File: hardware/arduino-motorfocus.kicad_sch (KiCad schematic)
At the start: 23 parts, among them J1 Motor, J2 PWR_MOTOR, J3 Debug, J4 I2C, J5 STEPS, J6 ULN2003A, J7 PWR_MOTOR, SW1 IN, SW2 OUT, SW3 WIN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

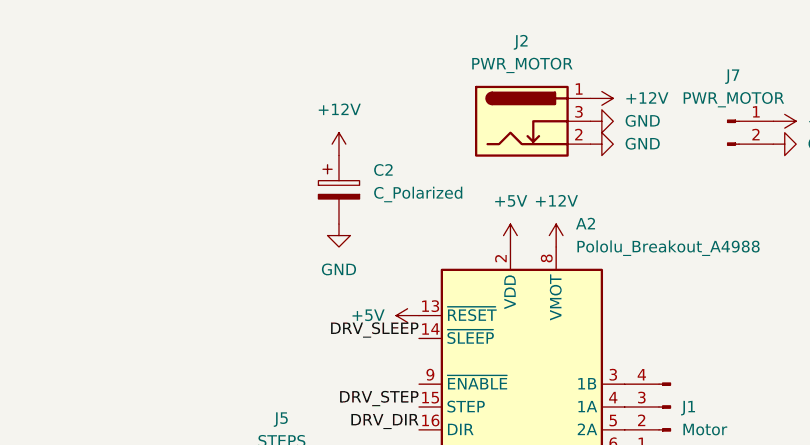
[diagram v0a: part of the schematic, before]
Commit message: Added simple PCB project and doc
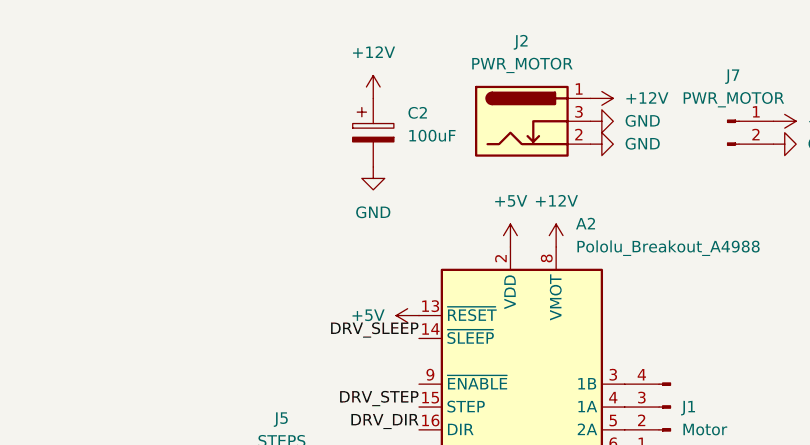
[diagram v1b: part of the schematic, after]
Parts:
- C2: value C_Polarized -> 100uF
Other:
- moved on the sheet: C2
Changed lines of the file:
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@@
     )
   )
-  (symbol (lib_id "Device:C_Polarized") (at 199.39 39.37 0) (unit 1)
-    (in_bom yes) (on_board yes) (dnp no) (fields_autoplaced)
-    (property "Reference" "C2" (at 203.2 37.211 0)
-      (effects (font (size 1.27 1.27)) (justify left))
-    )
-    (property "Value" "C_Polarized" (at 203.2 39.751 0)
-      (effects (font (size 1.27 1.27)) (justify left))
-    )
-    (property "Footprint" "Capacitor_SMD:CP_Elec_6.3x5.9" (at 200.3552 43.18 0)
-      (effects (font (size 1.27 1.27)) hide)
-    )
-    (property "Datasheet" "~" (at 199.39 39.37 0)
+  (symbol (lib_id "Device:C_Polarized") (at 203.2 33.02 0) (unit 1)
+    (in_bom yes) (on_board yes) (dnp no) (fields_autoplaced)
+    (property "Reference" "C2" (at 207.01 30.861 0)
+      (effects (font (size 1.27 1.27)) (justify left))
+    )
+    (property "Value" "100uF" (at 207.01 33.401 0)
+      (effects (font (size 1.27 1.27)) (justify left))
+    )
+    (property "Footprint" "Capacitor_SMD:CP_Elec_6.3x5.9" (at 204.1652 36.83 0)
+      (effects (font (size 1.27 1.27)) hide)
+    )
+    (property "Datasheet" "~" (at 203.2 33.02 0)
       (effects (font (size 1.27 1.27)) hide)
     )
@@
     )
   )
-  (symbol (lib_id "power:GND") (at 199.39 43.18 0) (unit 1)
-    (in_bom yes) (on_board yes) (dnp no) (fields_autoplaced)
-    (property "Reference" "#PWR019" (at 199.39 49.53 0)
-      (effects (font (size 1.27 1.27)) hide)
-    )
-    (property "Value" "GND" (at 199.39 48.26 0)
-      (effects (font (size 1.27 1.27)))
-    )
-    (property "Footprint" "" (at 199.39 43.18 0)
-      (effects (font (size 1.27 1.27)) hide)
-    )
-    (property "Datasheet" "" (at 199.39 43.18 0)
+  (symbol (lib_id "power:GND") (at 203.2 36.83 0) (unit 1)
+    (in_bom yes) (on_board yes) (dnp no) (fields_autoplaced)
+    (property "Reference" "#PWR019" (at 203.2 43.18 0)
+      (effects (font (size 1.27 1.27)) hide)
+    )
+    (property "Value" "GND" (at 203.2 41.91 0)
+      (effects (font (size 1.27 1.27)))
+    )
+    (property "Footprint" "" (at 203.2 36.83 0)
+      (effects (font (size 1.27 1.27)) hide)
+    )
+    (property "Datasheet" "" (at 203.2 36.83 0)
       (effects (font (size 1.27 1.27)) hide)
     )
@@
       (effects (font (size 1.27 1.27)) hide)
     )
-    (property "Datasheet" "~" (at 220.98 32.766 0)
+    (property "Datasheet" "https://de.aliexpress.com/item/1005002561919358.html" (at 220.98 32.766 0)
       (effects (font (size 1.27 1.27)) hide)
     )
@@
     )
   )
-  (symbol (lib_id "power:+12V") (at 199.39 35.56 0) (unit 1)
-    (in_bom yes) (on_board yes) (dnp no) (fields_autoplaced)
-    (property "Reference" "#PWR018" (at 199.39 39.37 0)
-      (effects (font (size 1.27 1.27)) hide)
-    )
-    (property "Value" "+12V" (at 199.39 30.48 0)
-      (effects (font (size 1.27 1.27)))
-    )
-    (property "Footprint" "" (at 199.39 35.56 0)
-      (effects (font (size 1.27 1.27)) hide)
-    )
-    (property "Datasheet" "" (at 199.39 35.56 0)
+  (symbol (lib_id "power:+12V") (at 203.2 29.21 0) (unit 1)
+    (in_bom yes) (on_board yes) (dnp no) (fields_autoplaced)
+    (property "Reference" "#PWR018" (at 203.2 33.02 0)
+      (effects (font (size 1.27 1.27)) hide)
+    )
+    (property "Value" "+12V" (at 203.2 24.13 0)
+      (effects (font (size 1.27 1.27)))
+    )
+    (property "Footprint" "" (at 203.2 29.21 0)
+      (effects (font (size 1.27 1.27)) hide)
+    )
+    (property "Datasheet" "" (at 203.2 29.21 0)
       (effects (font (size 1.27 1.27)) hide)
     )
@@
       (effects (font (size 1.27 1.27)) hide)
     )
-    (property "Datasheet" "~" (at 76.2 101.6 0)
-      (effects (font (size 1.27 1.27)) hide)
-    )
+    (property "Datasheet" "https://de.aliexpress.com/item/1005003399827077.html" (at 76.2 101.6 0)
+      (effects (font (size 1.27 1.27)) hide)
+    )
